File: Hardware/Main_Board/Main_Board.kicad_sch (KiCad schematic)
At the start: 0 parts

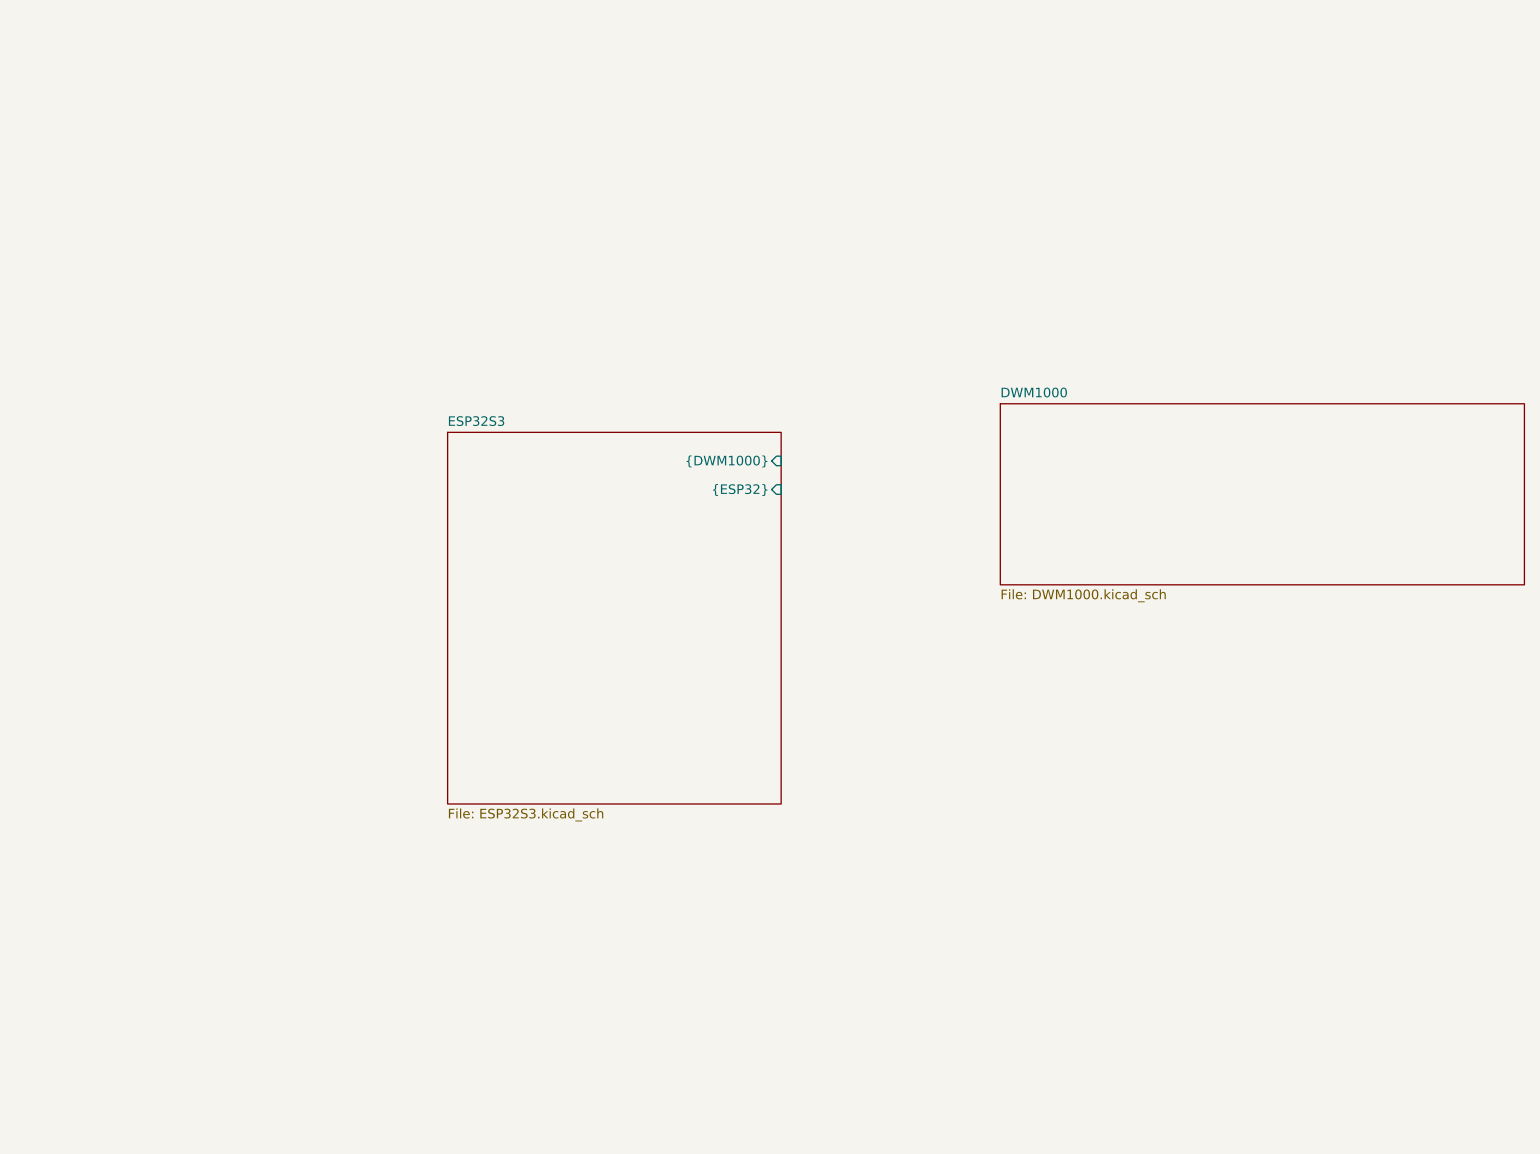
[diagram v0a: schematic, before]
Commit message: added 2 more sheets
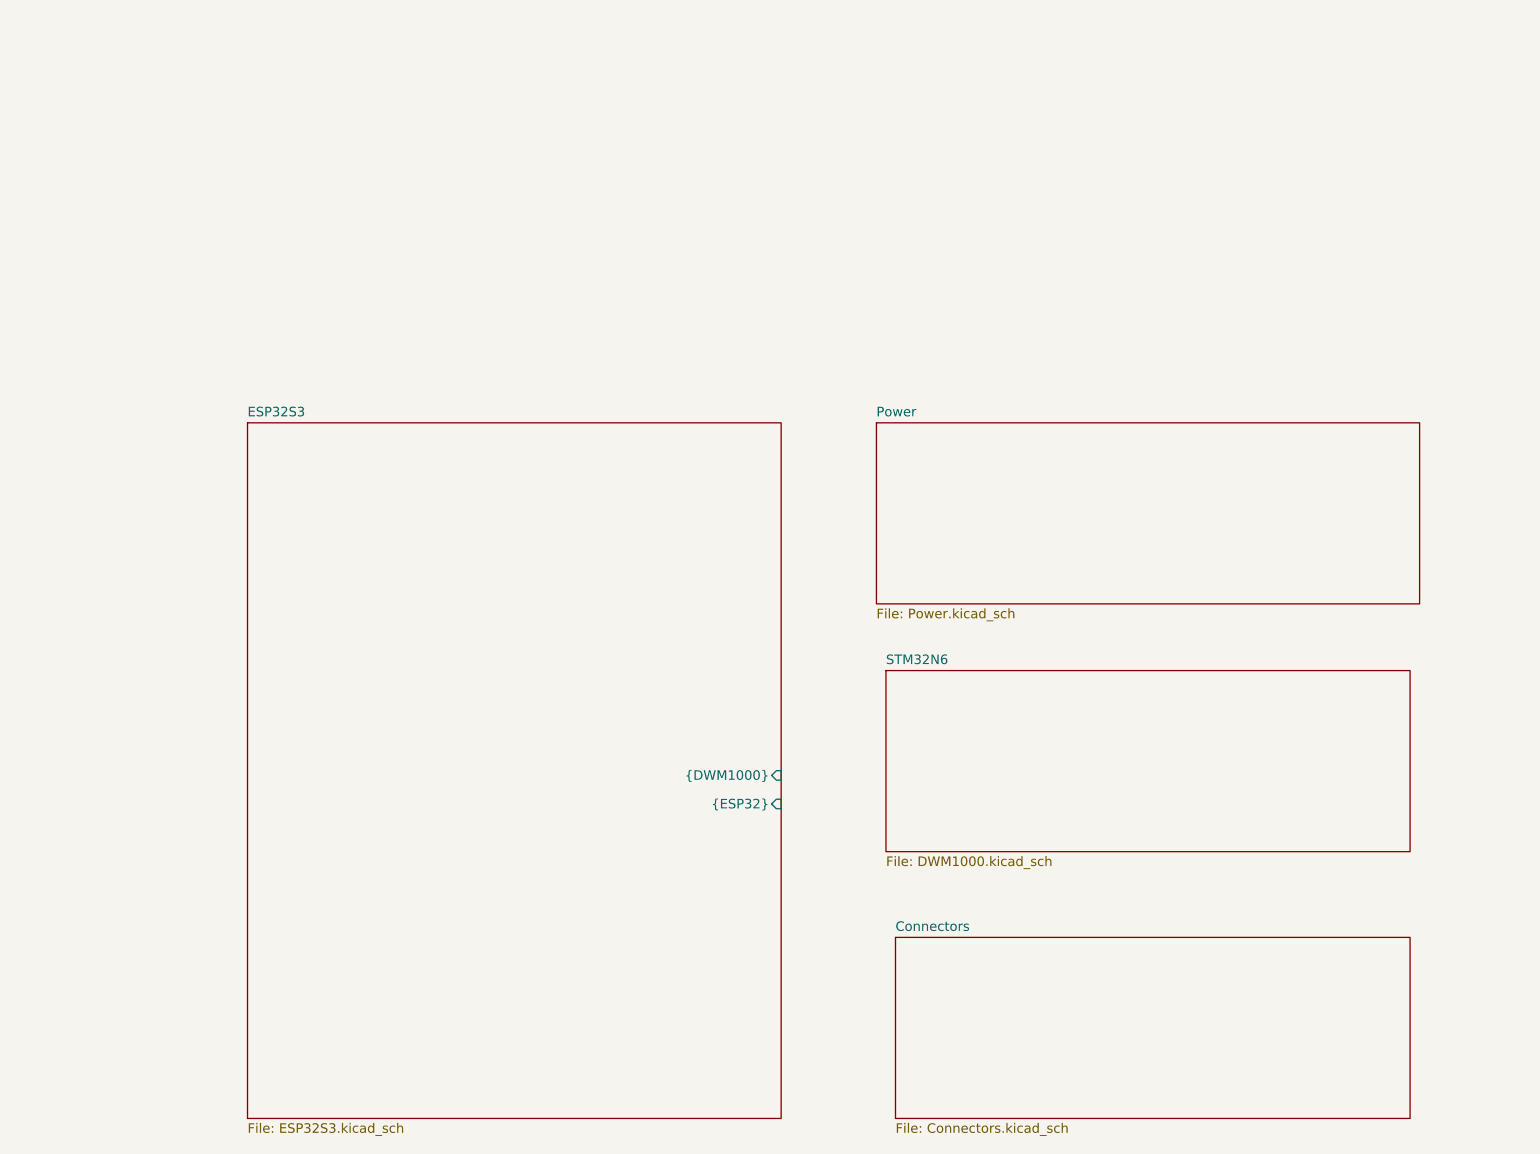
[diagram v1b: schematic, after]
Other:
- sheet DWM1000 renamed STM32N6
- added sheet Connectors (Connectors.kicad_sch)
- added sheet Power (Power.kicad_sch)
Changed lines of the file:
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@@
 	)
 	(sheet
-		(at 148.59 67.31)
+		(at 134.62 138.43)
+		(size 68.58 24.13)
+		(exclude_from_sim no)
+		(in_bom yes)
+		(on_board yes)
+		(dnp no)
+		(fields_autoplaced yes)
+		(stroke
+			(width 0.1524)
+			(type solid)
+		)
+		(fill
+			(color 0 221 221 1.0000)
+		)
+		(property "Sheetname" "Connectors"
+			(at 134.62 137.7184 0)
+			(effects
+				(font
+					(size 1.27 1.27)
+				)
+				(justify left bottom)
+			)
+		)
+		(property "Sheetfile" "Connectors.kicad_sch"
+			(at 134.62 163.1446 0)
+			(effects
+				(font
+					(size 1.27 1.27)
+				)
+				(justify left top)
+			)
+		)
+		(instances
+			(project "Main_Board"
+				(path "/3bfaeaa6-4337-4b5f-9f42-0e28df6ecb69"
+					(page "5")
+				)
+			)
+		)
+	)
+	(sheet
+		(at 133.35 102.87)
 		(size 69.85 24.13)
 		(exclude_from_sim no)
@@
 			(color 0 221 221 1.0000)
 		)
-		(property "Sheetname" "DWM1000"
-			(at 148.59 66.5984 0)
+		(property "Sheetname" "STM32N6"
+			(at 133.35 102.1584 0)
 			(effects
 				(font
@@
 		)
 		(property "Sheetfile" "DWM1000.kicad_sch"
-			(at 148.59 92.0246 0)
+			(at 133.35 127.5846 0)
 			(effects
 				(font
@@
 		)
 		(instances
-			(project "mainboarddesign"
+			(project "Main_Board"
 				(path "/3bfaeaa6-4337-4b5f-9f42-0e28df6ecb69"
 					(page "3")
@@
 	)
 	(sheet
-		(at 74.93 71.12)
-		(size 44.45 49.53)
+		(at 132.08 69.85)
+		(size 72.39 24.13)
+		(exclude_from_sim no)
+		(in_bom yes)
+		(on_board yes)
+		(dnp no)
+		(fields_autoplaced yes)
+		(stroke
+			(width 0.1524)
+			(type solid)
+		)
+		(fill
+			(color 0 221 221 1.0000)
+		)
+		(property "Sheetname" "Power"
+			(at 132.08 69.1384 0)
+			(effects
+				(font
+					(size 1.27 1.27)
+				)
+				(justify left bottom)
+			)
+		)
+		(property "Sheetfile" "Power.kicad_sch"
+			(at 132.08 94.5646 0)
+			(effects
+				(font
+					(size 1.27 1.27)
+				)
+				(justify left top)
+			)
+		)
+		(instances
+			(project "Main_Board"
+				(path "/3bfaeaa6-4337-4b5f-9f42-0e28df6ecb69"
+					(page "4")
+				)
+			)
+		)
+	)
+	(sheet
+		(at 48.26 69.85)
+		(size 71.12 92.71)
 		(exclude_from_sim no)
 		(in_bom yes)
@@
 		)
 		(property "Sheetname" "ESP32S3"
-			(at 74.93 70.4084 0)
+			(at 48.26 69.1384 0)
 			(effects
 				(font
@@
 		)
 		(property "Sheetfile" "ESP32S3.kicad_sch"
-			(at 74.93 121.2346 0)
+			(at 48.26 163.1446 0)
 			(effects
 				(font
@@
 		)
 		(pin "{DWM1000}" input
-			(at 119.38 74.93 0)
+			(at 119.38 116.84 0)
 			(effects
 				(font
@@
 		)
 		(pin "{ESP32}" input
-			(at 119.38 78.74 0)
+			(at 119.38 120.65 0)
 			(effects
 				(font
@@
 		)
 		(instances
-			(project "mainboarddesign"
+			(project "Main_Board"
 				(path "/3bfaeaa6-4337-4b5f-9f42-0e28df6ecb69"
 					(page "2")

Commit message: Mixed in all of Layth's work, and added extra sheets
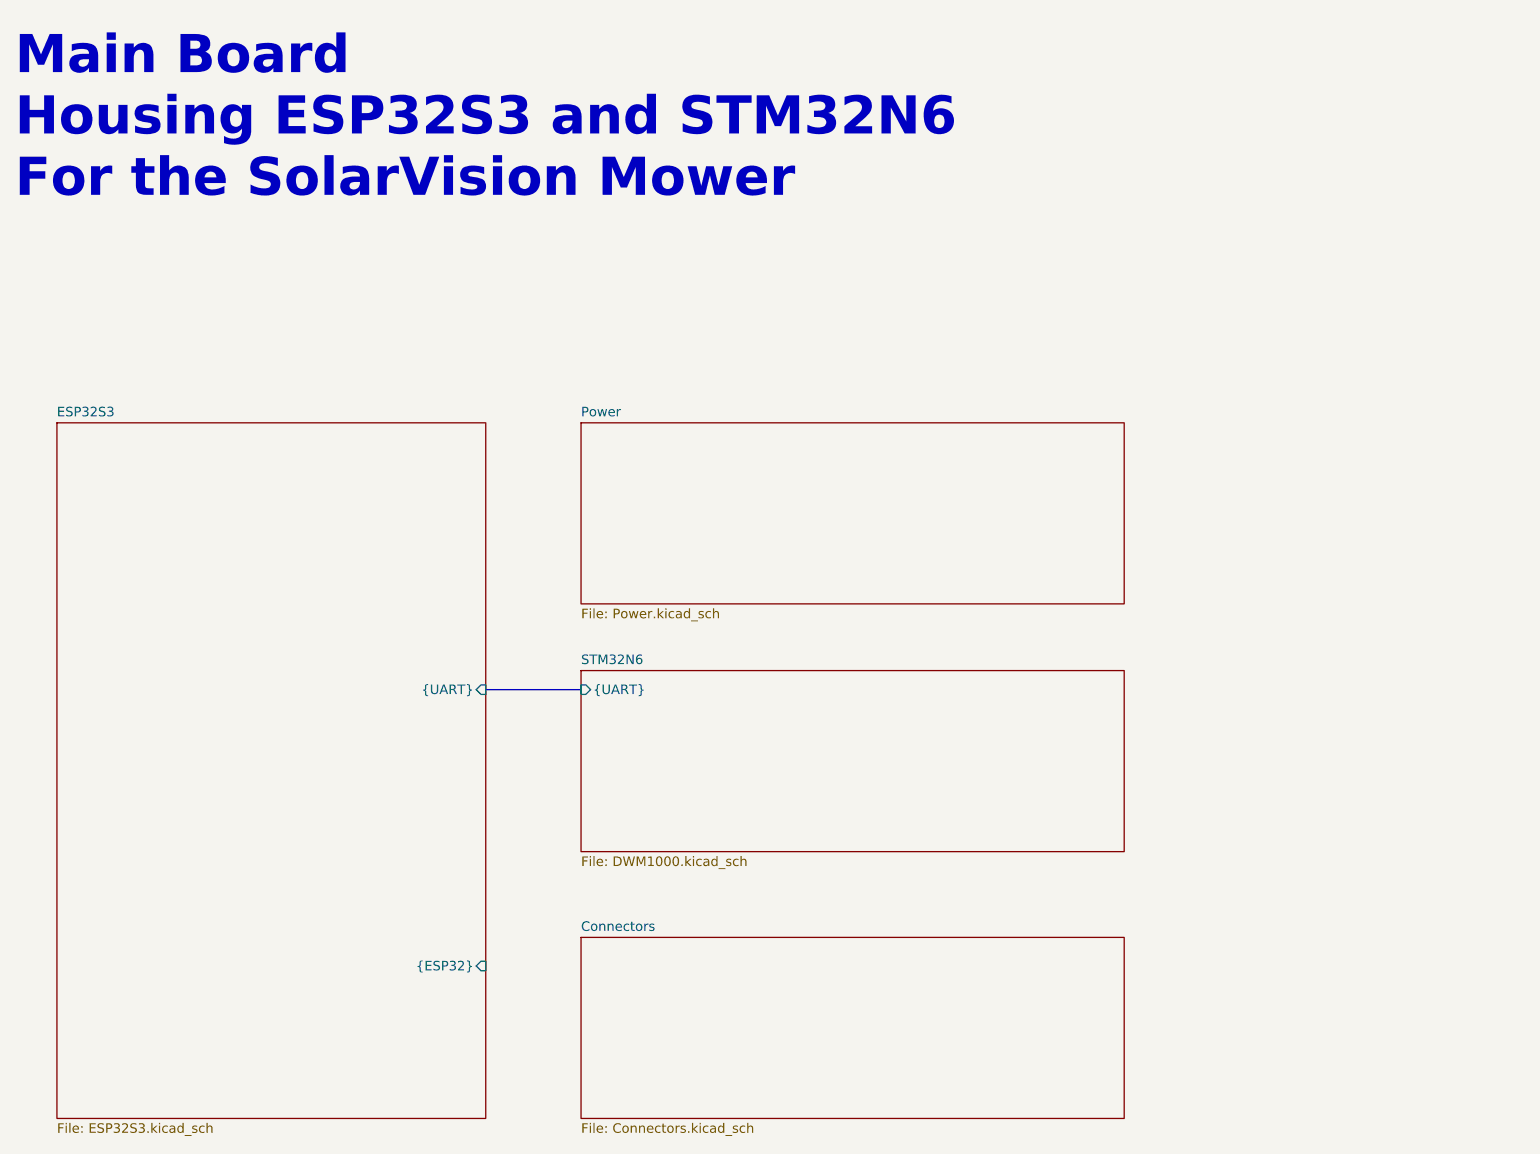
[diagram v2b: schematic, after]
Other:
- sheet ESP32S3 ports: added {UART}; removed {DWM1000}
- sheet STM32N6 ports: added {UART}; removed none
- note added: "Main Board Housing ESP32S3 and STM32N6 For the SolarVision Mower"
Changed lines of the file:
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@@
 		(members "GPIO[0..48]" "RST")
 	)
-	(sheet
-		(at 134.62 138.43)
-		(size 68.58 24.13)
+	(text "Main Board\nHousing ESP32S3 and STM32N6\nFor the SolarVision Mower"
+		(exclude_from_sim no)
+		(at 17.272 18.034 0)
+		(effects
+			(font
+				(size 5.08 5.08)
+				(thickness 1.016)
+				(bold yes)
+			)
+			(justify left top)
+		)
+	)
+	(bus
+		(pts
+			(xy 80.01 105.41) (xy 92.71 105.41)
+		)
+		(stroke
+			(width 0)
+			(type default)
+		)
+	)
+	(sheet
+		(at 92.71 138.43)
+		(size 72.39 24.13)
 		(exclude_from_sim no)
 		(in_bom yes)
@@
 		)
 		(property "Sheetname" "Connectors"
-			(at 134.62 137.7184 0)
+			(at 92.71 137.7184 0)
 			(effects
 				(font
@@
 		)
 		(property "Sheetfile" "Connectors.kicad_sch"
-			(at 134.62 163.1446 0)
+			(at 92.71 163.1446 0)
 			(effects
 				(font
@@
 	)
 	(sheet
-		(at 133.35 102.87)
-		(size 69.85 24.13)
+		(at 92.71 102.87)
+		(size 72.39 24.13)
 		(exclude_from_sim no)
 		(in_bom yes)
@@
 		)
 		(property "Sheetname" "STM32N6"
-			(at 133.35 102.1584 0)
+			(at 92.71 102.1584 0)
 			(effects
 				(font
@@
 		)
 		(property "Sheetfile" "DWM1000.kicad_sch"
-			(at 133.35 127.5846 0)
-			(effects
-				(font
-					(size 1.27 1.27)
-				)
-				(justify left top)
+			(at 92.71 127.5846 0)
+			(effects
+				(font
+					(size 1.27 1.27)
+				)
+				(justify left top)
+			)
+		)
+		(pin "{UART}" input
+			(at 92.71 105.41 180)
+			(effects
+				(font
+					(size 1.27 1.27)
+				)
+				(justify left)
+			)
+		)
+		(instances
+			(project "Main_Board"
+				(path "/3bfaeaa6-4337-4b5f-9f42-0e28df6ecb69"
+					(page "4")
+				)
+			)
+		)
+	)
+	(sheet
+		(at 92.71 69.85)
+		(size 72.39 24.13)
+		(exclude_from_sim no)
+		(in_bom yes)
+		(on_board yes)
+		(dnp no)
+		(fields_autoplaced yes)
+		(stroke
+			(width 0.1524)
+			(type solid)
+		)
+		(fill
+			(color 0 221 221 1.0000)
+		)
+		(property "Sheetname" "Power"
+			(at 92.71 69.1384 0)
+			(effects
+				(font
+					(size 1.27 1.27)
+				)
+				(justify left bottom)
+			)
+		)
+		(property "Sheetfile" "Power.kicad_sch"
+			(at 92.71 94.5646 0)
+			(effects
+				(font
+					(size 1.27 1.27)
+				)
+				(justify left top)
+			)
+		)
+		(instances
+			(project "Main_Board"
+				(path "/3bfaeaa6-4337-4b5f-9f42-0e28df6ecb69"
+					(page "2")
+				)
+			)
+		)
+	)
+	(sheet
+		(at 22.86 69.85)
+		(size 57.15 92.71)
+		(exclude_from_sim no)
+		(in_bom yes)
+		(on_board yes)
+		(dnp no)
+		(fields_autoplaced yes)
+		(stroke
+			(width 0.1524)
+			(type solid)
+		)
+		(fill
+			(color 0 221 221 1.0000)
+		)
+		(property "Sheetname" "ESP32S3"
+			(at 22.86 69.1384 0)
+			(effects
+				(font
+					(size 1.27 1.27)
+				)
+				(justify left bottom)
+			)
+		)
+		(property "Sheetfile" "ESP32S3.kicad_sch"
+			(at 22.86 163.1446 0)
+			(effects
+				(font
+					(size 1.27 1.27)
+				)
+				(justify left top)
+			)
+		)
+		(pin "{ESP32}" input
+			(at 80.01 142.24 0)
+			(effects
+				(font
+					(size 1.27 1.27)
+				)
+				(justify right)
+			)
+		)
+		(pin "{UART}" input
+			(at 80.01 105.41 0)
+			(effects
+				(font
+					(size 1.27 1.27)
+				)
+				(justify right)
 			)
 		)
@@
 				)
 			)
-		)
-	)
-	(sheet
-		(at 132.08 69.85)
-		(size 72.39 24.13)
-		(exclude_from_sim no)
-		(in_bom yes)
-		(on_board yes)
-		(dnp no)
-		(fields_autoplaced yes)
-		(stroke
-			(width 0.1524)
-			(type solid)
-		)
-		(fill
-			(color 0 221 221 1.0000)
-		)
-		(property "Sheetname" "Power"
-			(at 132.08 69.1384 0)
-			(effects
-				(font
-					(size 1.27 1.27)
-				)
-				(justify left bottom)
-			)
-		)
-		(property "Sheetfile" "Power.kicad_sch"
-			(at 132.08 94.5646 0)
-			(effects
-				(font
-					(size 1.27 1.27)
-				)
-				(justify left top)
-			)
-		)
-		(instances
-			(project "Main_Board"
-				(path "/3bfaeaa6-4337-4b5f-9f42-0e28df6ecb69"
-					(page "4")
-				)
-			)
-		)
-	)
-	(sheet
-		(at 48.26 69.85)
-		(size 71.12 92.71)
-		(exclude_from_sim no)
-		(in_bom yes)
-		(on_board yes)
-		(dnp no)
-		(fields_autoplaced yes)
-		(stroke
-			(width 0.1524)
-			(type solid)
-		)
-		(fill
-			(color 0 221 221 1.0000)
-		)
-		(property "Sheetname" "ESP32S3"
-			(at 48.26 69.1384 0)
-			(effects
-				(font
-					(size 1.27 1.27)
-				)
-				(justify left bottom)
-			)
-		)
-		(property "Sheetfile" "ESP32S3.kicad_sch"
-			(at 48.26 163.1446 0)
-			(effects
-				(font
-					(size 1.27 1.27)
-				)
-				(justify left top)
-			)
-		)
-		(pin "{DWM1000}" input
-			(at 119.38 116.84 0)
-			(effects
-				(font
-					(size 1.27 1.27)
-				)
-				(justify right)
-			)
-		)
-		(pin "{ESP32}" input
-			(at 119.38 120.65 0)
-			(effects
-				(font
-					(size 1.27 1.27)
-				)
-				(justify right)
-			)
-		)
-		(instances
-			(project "Main_Board"
-				(path "/3bfaeaa6-4337-4b5f-9f42-0e28df6ecb69"
-					(page "2")
-				)
-			)

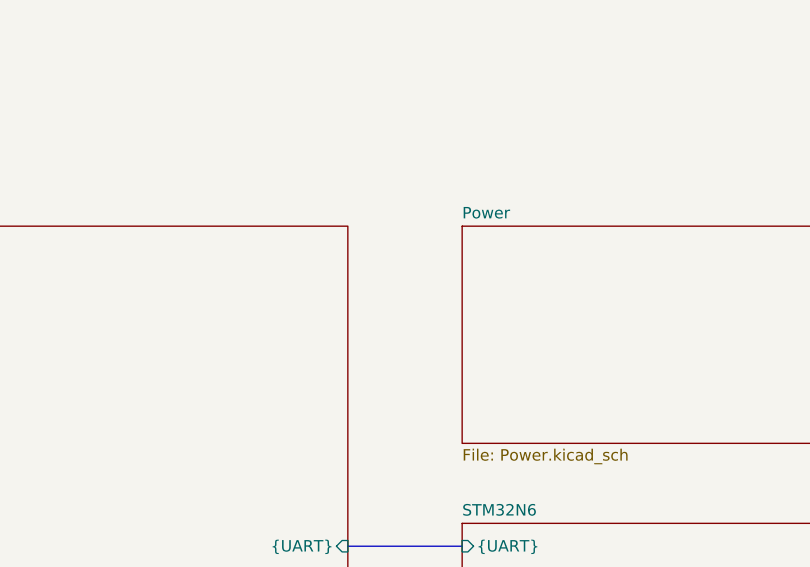
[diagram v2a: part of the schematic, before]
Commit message: On behalf of Panuha and Layth: Added inital schematics for Main Board
- Added initial power units, 3v3 LDO remains
- Added buses for the ESP, UWB, and STM boards
- Connector sheet, footprint assignment, ERC check, etc remains.
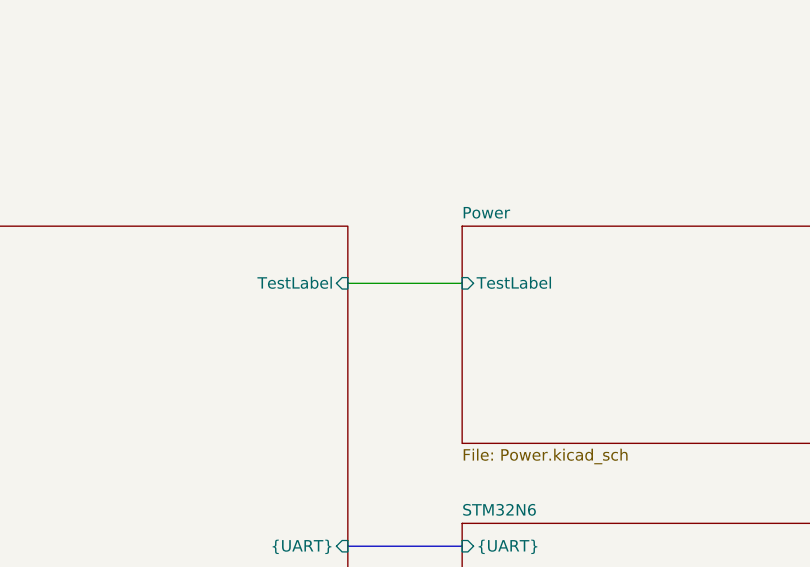
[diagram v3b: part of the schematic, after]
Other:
- sheet ESP32S3 ports: added TestLabel; removed none
- sheet Power ports: added TestLabel; removed none
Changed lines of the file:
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@@
+		)
+	)
+	(wire
+		(pts
+			(xy 80.01 76.2) (xy 92.71 76.2)
+		)
+		(stroke
+			(width 0)
+			(type default)
 		)
 	)
@@
 			)
 		)
+		(pin "TestLabel" input
+			(at 92.71 76.2 180)
+			(effects
+				(font
+					(size 1.27 1.27)
+				)
+				(justify left)
+			)
+		)
 		(instances
 			(project "Main_Board"
@@
 			(effects
 				(font
+					(size 1.27 1.27)
+				)
+				(justify right)
+			)
+		)
+		(pin "TestLabel" input
+			(at 80.01 76.2 0)
+			(effects
+				(font
